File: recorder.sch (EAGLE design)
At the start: 47 parts, among them M1 ELECTRET_MICROPHON-WM-61A, T1 MMBT3904 NPN, Y1 4.096MHz

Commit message: Oops.. forgot to re-add *.sch and *.epf files to last commit. Everything should be up to date now.
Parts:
- removed JP8: None, SparkFun-Connectors:M03PTH
- removed Y1: 4.096MHz, SparkFun-FreqCtrl:CRYSTALHC49US
- added Q1: 4.096MHz, adafruit:CRYSTALSM49
- C1: value 0.1uF -> 47uF
- C10: device rcl:C-USC0402 -> rcl:C-USC1206
- C11: value 0.01uF -> 0.1uF
- C12: value 0.001uF -> 0.1uF
- C15: value 47uF -> 0.1uF; device rcl:C-USC1206 -> rcl:C-USC0402
- C16: value 0.1uF -> 27pF
- C17: value 0.1uF -> 47uF; device rcl:C-USC0402 -> rcl:C-USC1206
- C18: value 47uF -> 27pF; device rcl:C-USC1206 -> rcl:C-USC0402
- C19: device rcl:C-USC0603 -> rcl:C-USC0402
- C2: value 220uF -> 0.01uF
- C4: value 0.1uF -> 0.001uF
- C6: device rcl:C-USC0402 -> rcl:C-USC0603
- C7: value 27pF -> 220uF
- C8: value 27pF -> 0.1uF
- JP1: value None -> M02PTH; device SparkFun-Connectors:M04POLAR -> SparkFun-Connectors:M02PTH
- JP2: value 3.5mm -> (none); device SparkFun-Connectors:AUDIO-JACKPTH -> SparkFun-Connectors:M04PTH
- JP3: value None -> (none); device SparkFun-Connectors:M04POLAR -> SparkFun-Connectors:M04PTH
- JP4: value M02PTH4 -> (none); device SparkFun-Connectors:M02PTH4 -> SparkFun-Connectors:AUDIO-JACKSMD2
- JP5: value M02PTH4 -> (none); device SparkFun-Connectors:M02PTH4 -> SparkFun-Connectors:M04PTH
- JP6: device SparkFun-Connectors:M04POLAR -> SparkFun-Connectors:M03PTH
- JP7: value Speaker -> M02PTH; device SparkFun-Connectors:M02PTH4 -> SparkFun-Connectors:M02PTH
- R1, R2: value 10kohm -> 5.6kohm; device rcl:R-US_R0201 -> rcl:R-US_R0402; MF AVX CORPORATION -> (none); MPN 0402ZD104KAT2A -> (none); OC_NEWARK 81C8514 -> (none)
- R10: value 4.7kohm -> 1Mohm
- R11: value 270ohms -> 10kohm
- R12: value 1.5kohm -> 430ohm; device rcl:R-US_R0201 -> rcl:R-US_R0402; MF AVX CORPORATION -> (none); MPN 0402ZD104KAT2A -> (none); OC_NEWARK 81C8514 -> (none)
- R13: value 1.5kohm -> 0 ohm; device rcl:R-US_R0201 -> rcl:R-US_R0603; MF AVX CORPORATION -> (none); MPN 0402ZD104KAT2A -> (none); OC_NEWARK 81C8514 -> (none)
- R14: value 1.5kohm -> 80.6kohm; device rcl:R-US_R0201 -> rcl:R-US_R0402; MF AVX CORPORATION -> (none); MPN 0402ZD104KAT2A -> (none); OC_NEWARK 81C8514 -> (none)
- R3: value 0 ohm -> 1.5kohm; device rcl:R-US_R0603 -> rcl:R-US_R0201; MF (none) -> AVX CORPORATION; MPN (none) -> 0402ZD104KAT2A; OC_NEWARK (none) -> 81C8514
- R4, R5: value 5.6kohm -> 1.5kohm; device rcl:R-US_R0402 -> rcl:R-US_R0201; MF (none) -> AVX CORPORATION; MPN (none) -> 0402ZD104KAT2A; OC_NEWARK (none) -> 81C8514
- R6: value 430ohm -> 4.7kohm; device rcl:R-US_R0402 -> rcl:R-US_R0201; MF (none) -> AVX CORPORATION; MPN (none) -> 0402ZD104KAT2A; OC_NEWARK (none) -> 81C8514
- R8: value 1Mohm -> 10kohm
- R9: value 80.6kohm -> 270ohms; device rcl:R-US_R0402 -> rcl:R-US_R0201; MF (none) -> AVX CORPORATION; MPN (none) -> 0402ZD104KAT2A; OC_NEWARK (none) -> 81C8514
- renumbered U$1 to U1
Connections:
- removed net N$10: C6.2, R10.1, R7.1
- removed net N$20: R15.1, U1.RDY/BSYB
- removed net N$6: C4.2, R6.1, T1.E
- removed net N$8: R11.2, R8.1, U1.XTALOUT
- new net N$3: C12.2, R6.1, R7.1
- new net RDY: R11.1, U1.RDY/BSYB
- new net XTALOUT: R10.1, R9.2, U1.XTALOUT
- net AGND: now also C19.2, C7.2, JP1.1, R12.1, R13.1, R2.1, R6.2, T1.E; no longer C2.2, C5.2, JP5.1, R10.2, R14.1, R3.1
- net AUDOUT: now also C19.1, R12.2; no longer C4.1, R6.2
- net AUXIN: now also C6.2; no longer C19.2
- net DGND: now also C1.2, C14.2, C15.2, C2.2, C4.2, C5.2, R11.2, R13.2, R14.2; no longer C10.2, C11.2, C12.2, C7.2, C8.2, R2.2, R3.2, R9.2
- net GPIO0: now also JP5.1; no longer JP3.1
- net GPIO1: now also JP5.2; no longer JP3.2
- net GPIO2: now also JP5.3; no longer JP3.3
- net GPIO3: now also JP5.4; no longer JP3.4
- net MIC+: now also C8.1; no longer C9.1
- net MIC-: now also C9.1; no longer C1.1
- net MISO: now also JP2.4; no longer JP6.4
- net MOSI: now also JP2.1; no longer JP6.1
- net N$1: now also C18.1, JP6.1, Q1.2, R10.2; no longer C8.1, JP8.1, R8.2, Y1.2
- net N$11: now also C12.1; no longer C6.1
- net N$19: now also C10.2, C11.2; no longer C14.2, C15.2
- net N$2: now also C16.1, Q1.1, R9.1; no longer C7.1, R11.1, Y1.1
- net N$21: now also C9.2, R5.2; no longer C1.2, R14.2
- net N$22: now also C8.2, R4.2; no longer C9.2, R12.2
- net N$28: now also C7.1, R3.1, R4.1; no longer C2.1, R12.1, R13.1
- net N$4: now also R8.2; no longer R1.2
- net N$5: now also JP1.2, R1.1; no longer JP5.2, R4.1
- net N$7: now also JP6.3, R14.1; no longer JP8.3, R9.1
- net N$9: now also C6.1, R1.2, R2.2; no longer C19.1, R4.2, R5.2
- net RESET: now also R15.1; no longer R2.1
- net SCK: now also JP3.3; no longer JP1.3
- net SCLK: now also JP2.3; no longer JP6.3
- net SDI: now also JP3.4; no longer JP1.4
- net SDO: now also JP3.1; no longer JP1.1
- net SPK+: now also JP4.SLEEVE; no longer JP2.SLEEVE, JP4.1
- net SPK-: now also JP4.LEFT; no longer JP2.LEFT, JP4.2
- net SSB: now also JP2.2; no longer JP6.2
- net VCCA: now also C10.1, C11.1, R3.2; no longer C14.1, C15.1, R13.2
- net VCCD: now also C1.1, C2.1, C4.1, R8.1; no longer C10.1, C11.1, C12.1, R1.1
- net VCCD_PWM: now also C14.1, C15.1; no longer C16.1, C18.1
- net WS: now also JP3.2; no longer JP1.2
- net XTALIN: now also JP6.2; no longer JP8.2
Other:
- note added: "Analog Side"
- note added: "Digital"
- note added: "Digital Side"
- note added: "Not Sure about this ???"
- moved on the sheet: C1, C10, C11, C12, C14, C15, C16, C17, C18, C19, C2, C3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

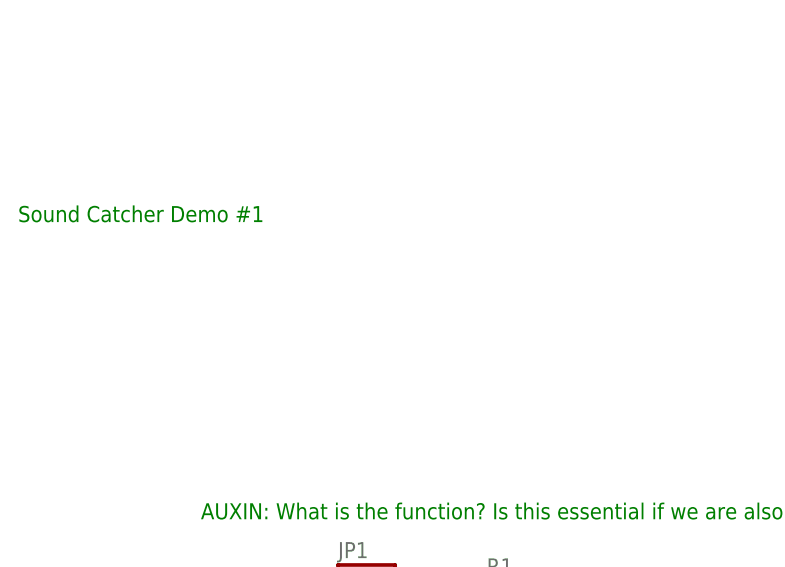
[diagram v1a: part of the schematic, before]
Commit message: rearranged dimensions of board
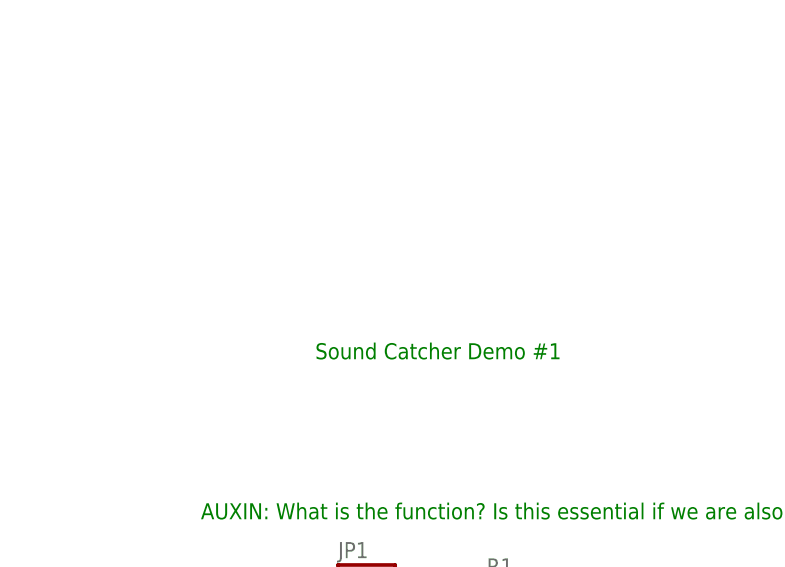
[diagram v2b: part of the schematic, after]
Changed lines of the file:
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@@
 <sheet>
 <plain>
-<text x="-111.76" y="182.88" size="1.778" layer="91">Sound Catcher Demo #1</text>
+<text x="-78.74" y="167.64" size="1.778" layer="91">Sound Catcher Demo #1</text>
 <text x="66.294" y="26.162" size="1.778" layer="91">Must be close to pins 17, 19 and 21.</text>
 <text x="-91.44" y="149.86" size="1.778" layer="91">AUXIN: What is the function? Is this essential if we are also using the MIC?</text>

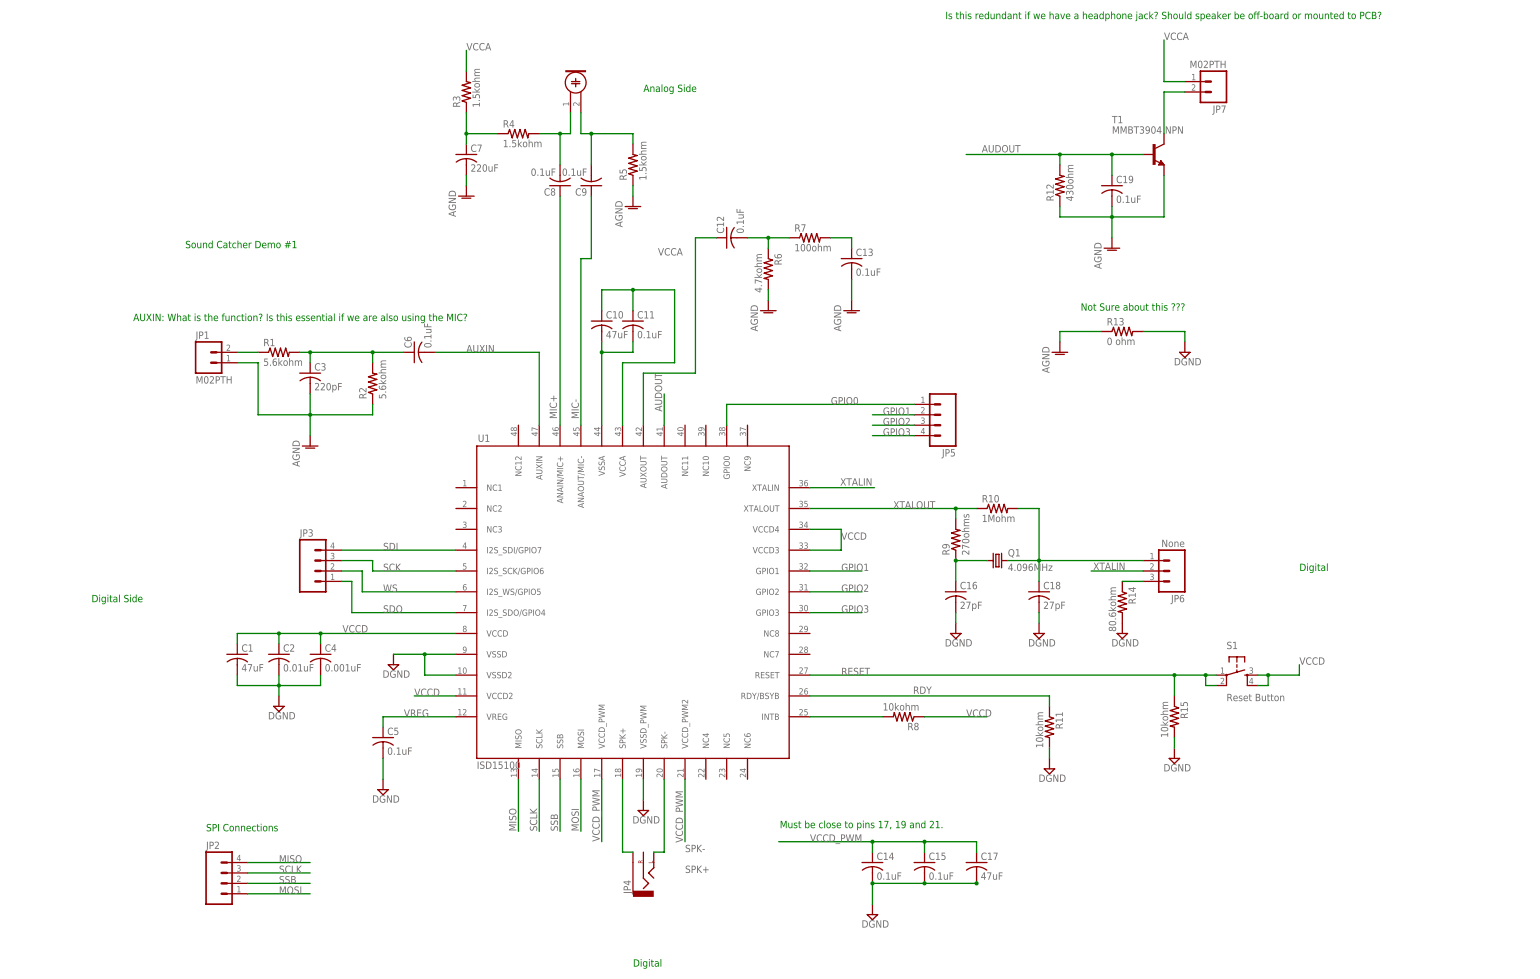
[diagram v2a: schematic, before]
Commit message: Began routing PCB traces. Almost finished but vias are not connected
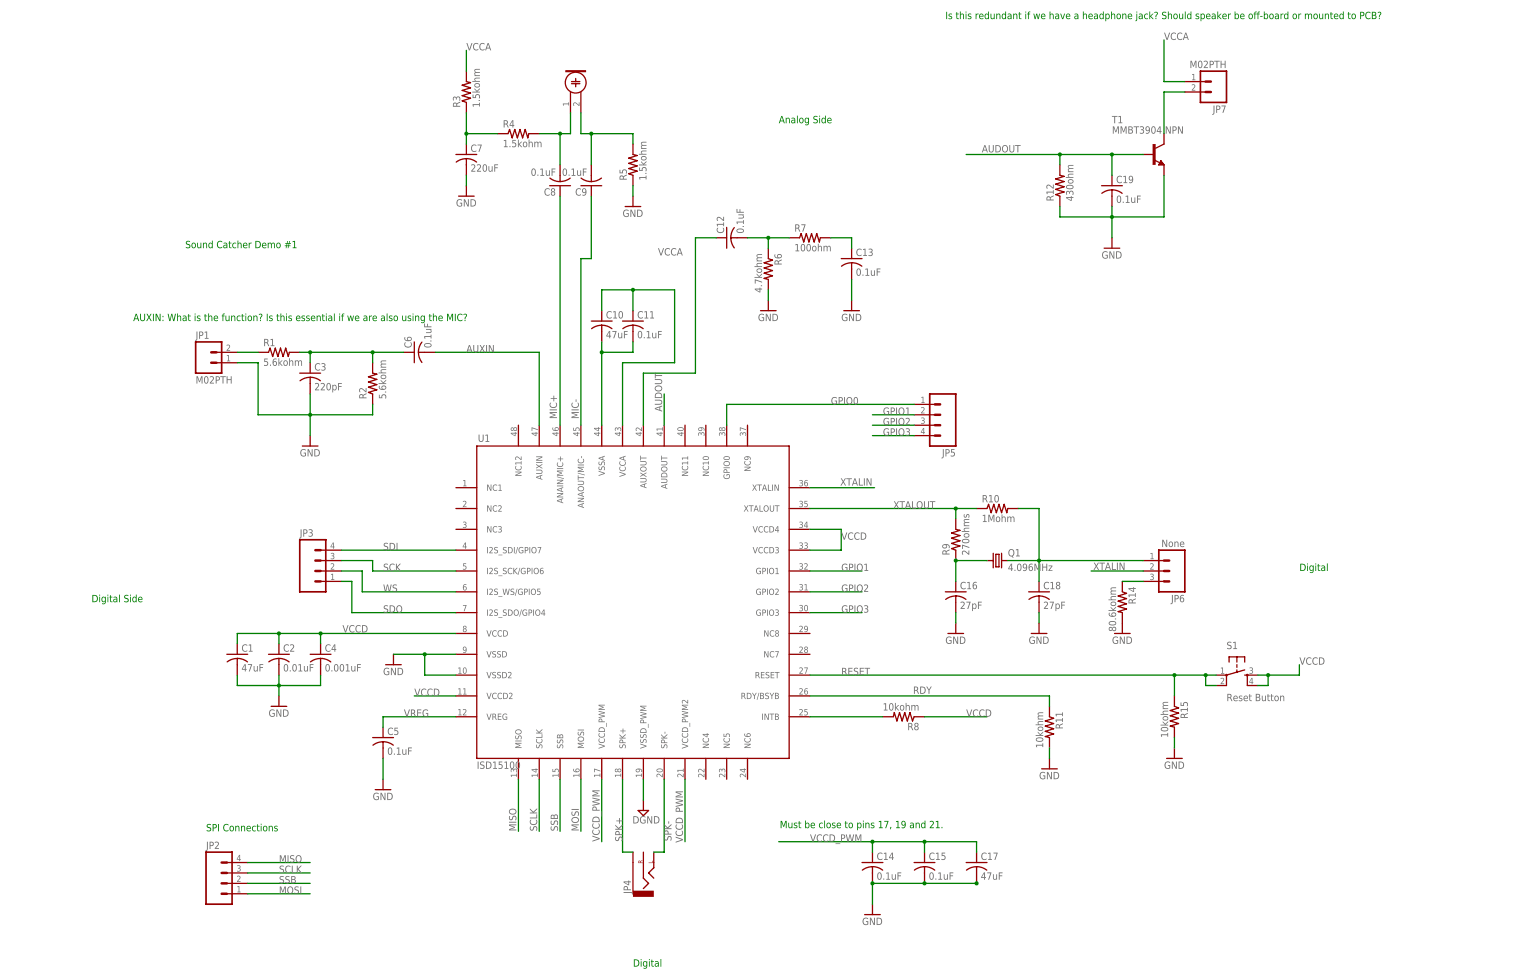
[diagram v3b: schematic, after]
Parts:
- removed R13: 0 ohm, rcl:R-US_R0603
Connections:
- removed net AGND: C13.2, C19.2, C3.2, C7.2, JP1.1, R12.1, R13.1, R2.1, R5.1, R6.2, T1.E
- new net GND: C1.2, C13.2, C14.2, C15.2, C16.2, C17.2, C18.2, C19.2, C2.2, C3.2, C4.2, C5.2, C7.2, JP1.1, R11.2, R12.1, R14.2, R15.2, R2.1, R5.1, R6.2, T1.E, U1.VSSD, U1.VSSD2
- net DGND: no longer C1.2, C14.2, C15.2, C16.2, C17.2, C18.2, C2.2, C4.2, C5.2, R11.2, R13.2, R14.2, R15.2, U1.VSSD, U1.VSSD2
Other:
- note removed: "Not Sure about this ???"

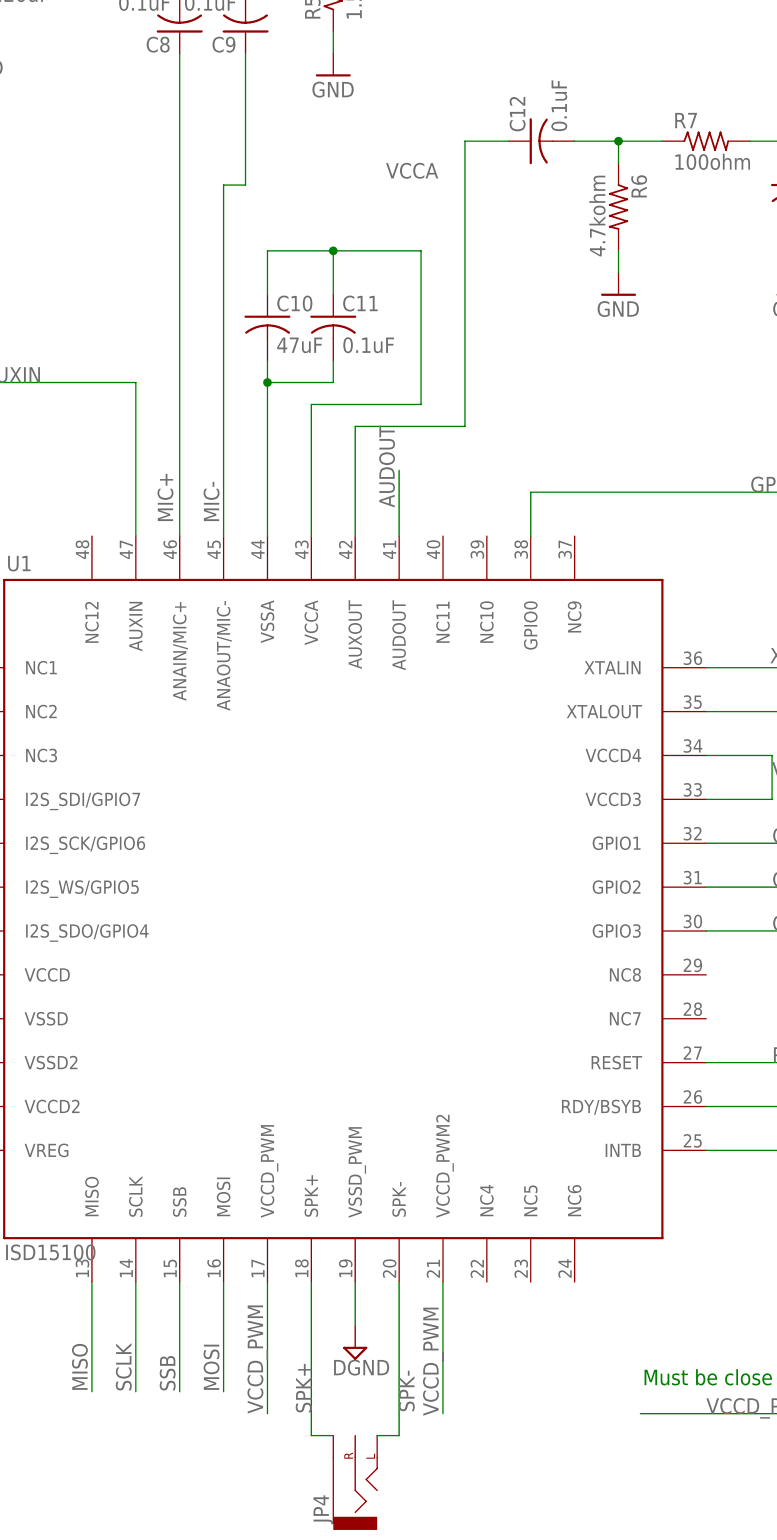
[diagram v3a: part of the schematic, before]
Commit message: Finished layout of PCB board. DRC mostly clean other than drill requirements, which can be adjusted
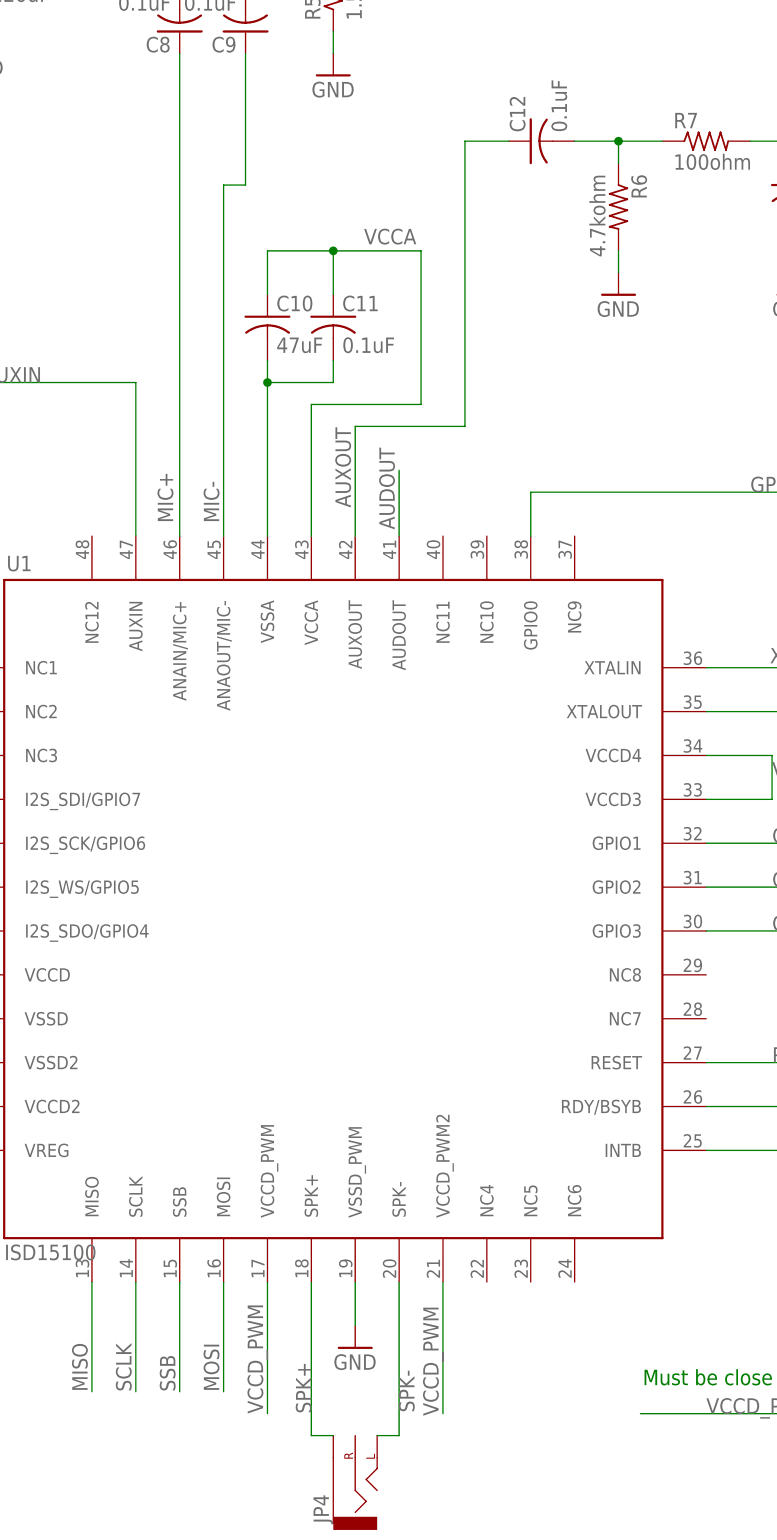
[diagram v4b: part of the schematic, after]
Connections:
- net N$11 renamed AUXOUT
- removed net DGND: U1.VSSD_PWM
- net GND: now also U1.VSSD_PWM
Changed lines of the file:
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@@
 <part name="C16" library="rcl" deviceset="C-US" device="C0402" value="27pF"/>
 <part name="C18" library="rcl" deviceset="C-US" device="C0402" value="27pF"/>
-<part name="SUPPLY4" library="supply2" deviceset="DGND" device=""/>
 <part name="C8" library="rcl" deviceset="C-US" device="C0402" value="0.1uF"/>
 <part name="C1" library="rcl" deviceset="C-US" device="C0402" value="47uF"/>
@@
 <part name="GND14" library="SparkFun-Aesthetics" deviceset="GND" device=""/>
 <part name="GND15" library="SparkFun-Aesthetics" deviceset="GND" device=""/>
+<part name="GND16" library="SparkFun-Aesthetics" deviceset="GND" device=""/>
 </parts>
 <sheets>
@@
 <instance part="C16" gate="G$1" x="109.22" y="83.82"/>
 <instance part="C18" gate="G$1" x="129.54" y="83.82"/>
-<instance part="SUPPLY4" gate="G$1" x="33.02" y="30.48"/>
 <instance part="C8" gate="G$1" x="12.7" y="182.88" rot="R180"/>
 <instance part="C1" gate="G$1" x="-66.04" y="68.58"/>
@@
 <instance part="GND14" gate="1" x="129.54" y="73.66"/>
 <instance part="GND15" gate="1" x="149.86" y="73.66"/>
+<instance part="GND16" gate="1" x="33.02" y="30.48"/>
 </instances>
 <busses>
 </busses>
 <nets>
-<net name="DGND" class="0">
-<segment>
-<pinref part="U1" gate="G$1" pin="VSSD_PWM"/>
-<pinref part="SUPPLY4" gate="G$1" pin="DGND"/>
-<wire x1="33.02" y1="38.1" x2="33.02" y2="33.02" width="0.1524" layer="91"/>
-</segment>
-</net>
 <net name="N$1" class="0">
 <segment>
@@
 </segment>
 </net>
-<net name="N$11" class="0">
+<net name="AUXOUT" class="0">
 <segment>
 <pinref part="U1" gate="G$1" pin="AUXOUT"/>
@@
 <pinref part="C12" gate="G$1" pin="1"/>
 <wire x1="45.72" y1="170.18" x2="50.8" y2="170.18" width="0.1524" layer="91"/>
+<label x="32.512" y="127.762" size="1.778" layer="95" rot="R90"/>
 </segment>
 </net>
@@
 </segment>
 </net>
-<net name="N$21" class="0">
+<net name="N$15" class="0">
 <segment>
 <pinref part="M1" gate="G$1" pin="2"/>
@@
 <wire x1="22.86" y1="157.48" x2="22.86" y2="152.4" width="0.1524" layer="91"/>
 <pinref part="C10" gate="G$1" pin="1"/>
-<label x="36.576" y="165.862" size="1.778" layer="95"/>
+<label x="34.036" y="158.242" size="1.778" layer="95"/>
 <wire x1="40.64" y1="157.48" x2="30.48" y2="157.48" width="0.1524" layer="91"/>
 <junction x="30.48" y="157.48"/>
@@
 <pinref part="U1" gate="G$1" pin="AUDOUT"/>
 <wire x1="38.1" y1="124.46" x2="38.1" y2="132.08" width="0.1524" layer="91"/>
-<label x="37.592" y="127.762" size="1.778" layer="95" rot="R90"/>
+<label x="37.592" y="125.222" size="1.778" layer="95" rot="R90"/>
 </segment>
 <segment>
@@
 <pinref part="GND15" gate="1" pin="GND"/>
 </segment>
-</net>
+<segment>
+<pinref part="U1" gate="G$1" pin="VSSD_PWM"/>
+<wire x1="33.02" y1="38.1" x2="33.02" y2="33.02" width="0.1524" layer="91"/>
+<pinref part="GND16" gate="1" pin="GND"/>
+</segment>
+</net>
